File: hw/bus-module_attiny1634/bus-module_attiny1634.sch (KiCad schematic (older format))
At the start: 31 parts, among them J1 CONN_5X2, J2 CONN_5X2, J3 CONN-ISP-6, J4 CONN_1, J5 CONN_1, J6 CONN_1, J7 CONN_1, U1 7,3728MHz, U2 25LCXXX, U3 ATTINY1634-SOIC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

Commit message: R2, R3, R4 100 Ohms
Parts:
- C1, C2, C3, C4, C5, C7, R1, R2, R3, R4, R5, R6: footprint Resistor:SM0805 -> Resistor:R_0805
- F1: footprint (none) -> Resistor:R_1206
- U3: footprint SO20L -> Housings_SOIC:SO20L
- U5: footprint AM1S-XXXX_SIL4 -> DCDC_Converter:AM1S-XXXX_SIL4
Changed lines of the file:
@@
 F 0 "C7" H 7950 2250 50  0000 L CNN
 F 1 "100nF" H 7900 2075 50  0000 C CNN
-F 2 "Resistor:SM0805" H 7900 2200 60  0001 C CNN
+F 2 "Resistor:R_0805" H 7900 2200 60  0001 C CNN
 F 3 "" H 7900 2200 60  0000 C CNN
 	1    7900 2200
@@
 F 0 "C5" H 5650 2250 50  0000 L CNN
 F 1 "100nF" H 5600 2350 50  0000 C CNN
-F 2 "Resistor:SM0805" H 5600 2200 60  0001 C CNN
+F 2 "Resistor:R_0805" H 5600 2200 60  0001 C CNN
 F 3 "" H 5600 2200 60  0000 C CNN
 	1    5600 2200
@@
 F 0 "C3" H 5050 5200 50  0000 L CNN
 F 1 "18pF" H 5000 5025 50  0000 C CNN
-F 2 "Resistor:SM0805" H 5000 5150 60  0001 C CNN
+F 2 "Resistor:R_0805" H 5000 5150 60  0001 C CNN
 F 3 "" H 5000 5150 60  0000 C CNN
 	1    5000 5150
@@
 F 0 "C2" H 5050 4750 50  0000 L CNN
 F 1 "18pF" H 5000 4575 50  0000 C CNN
-F 2 "Resistor:SM0805" H 5000 4700 60  0001 C CNN
+F 2 "Resistor:R_0805" H 5000 4700 60  0001 C CNN
 F 3 "" H 5000 4700 60  0000 C CNN
 	1    5000 4700
@@
 F 0 "C4" H 5250 6350 50  0000 L CNN
 F 1 "100nF" H 5200 6175 50  0000 C CNN
-F 2 "Resistor:SM0805" H 5200 6300 60  0001 C CNN
+F 2 "Resistor:R_0805" H 5200 6300 60  0001 C CNN
 F 3 "" H 5200 6300 60  0000 C CNN
 	1    5200 6300
@@
 F 0 "R4" H 4100 5700 50  0000 C CNN
 F 1 "100" H 4800 5700 50  0000 C CNN
-F 2 "Resistor:SM0805" H 4800 5700 60  0001 C CNN
+F 2 "Resistor:R_0805" H 4800 5700 60  0001 C CNN
 F 3 "" H 4800 5700 60  0000 C CNN
 	1    4800 5700
@@
 F 0 "R3" H 4100 5600 50  0000 C CNN
 F 1 "100" H 4800 5600 50  0000 C CNN
-F 2 "Resistor:SM0805" H 4800 5600 60  0001 C CNN
+F 2 "Resistor:R_0805" H 4800 5600 60  0001 C CNN
 F 3 "" H 4800 5600 60  0000 C CNN
 	1    4800 5600
@@
 F 0 "R2" H 4100 5500 50  0000 C CNN
 F 1 "100" H 4800 5500 50  0000 C CNN
-F 2 "Resistor:SM0805" H 4800 5500 60  0001 C CNN
+F 2 "Resistor:R_0805" H 4800 5500 60  0001 C CNN
 F 3 "" H 4800 5500 60  0000 C CNN
 	1    4800 5500
@@
 F 0 "R1" H 4550 6250 50  0000 C CNN
 F 1 "10k" H 4550 6350 50  0000 C CNN
-F 2 "Resistor:SM0805" H 4550 6350 60  0001 C CNN
+F 2 "Resistor:R_0805" H 4550 6350 60  0001 C CNN
 F 3 "" H 4550 6350 60  0000 C CNN
 	1    4550 6350
@@
 F 0 "R6" H 5900 6250 50  0000 C CNN
 F 1 "10k" H 5900 6350 50  0000 C CNN
-F 2 "Resistor:SM0805" H 5900 6350 60  0001 C CNN
+F 2 "Resistor:R_0805" H 5900 6350 60  0001 C CNN
 F 3 "" H 5900 6350 60  0000 C CNN
 	1    5900 6350
@@
 F 0 "C1" H 4950 2250 50  0000 L CNN
 F 1 "4,7nF" H 5000 2350 50  0000 C CNN
-F 2 "Resistor:SM0805" H 4900 2200 60  0001 C CNN
+F 2 "Resistor:R_0805" H 4900 2200 60  0001 C CNN
 F 3 "" H 4900 2200 60  0000 C CNN
 	1    4900 2200
@@
 F 0 "R5" H 4900 1800 50  0000 C CNN
 F 1 "10k" H 4900 1700 50  0000 C CNN
-F 2 "Resistor:SM0805" H 4900 1700 60  0001 C CNN
+F 2 "Resistor:R_0805" H 4900 1700 60  0001 C CNN
 F 3 "" H 4900 1700 60  0000 C CNN
 	1    4900 1700
@@
 F 0 "U3" H 5350 3600 50  0000 C CNN
 F 1 "ATTINY1634-SOIC" H 5350 3000 50  0000 C CNN
-F 2 "SO20L" H 5350 3600 25  0001 C CNN
+F 2 "Housings_SOIC:SO20L" H 5350 3600 25  0001 C CNN
 F 3 "" H 5350 3600 25  0001 C CNN
 	1    5350 3600
@@
 F 0 "F1" H 9200 1300 50  0000 C CNN
 F 1 "FUSE" H 9200 1100 50  0000 C CNN
-F 2 "" H 9200 1200 60  0000 C CNN
+F 2 "Resistor:R_1206" H 9200 1200 60  0001 C CNN
 F 3 "" H 9200 1200 60  0000 C CNN
 	1    9200 1200
@@
 F 0 "U5" H 8050 1715 50  0000 C CNN
 F 1 "AM1S-2405" H 8050 1624 50  0000 C CNN
-F 2 "AM1S-XXXX_SIL4" H 8050 1500 25  0001 C CNN
+F 2 "DCDC_Converter:AM1S-XXXX_SIL4" H 8050 1500 25  0001 C CNN
 F 3 "" H 7300 1300 25  0001 C CNN
 	1    8050 1300

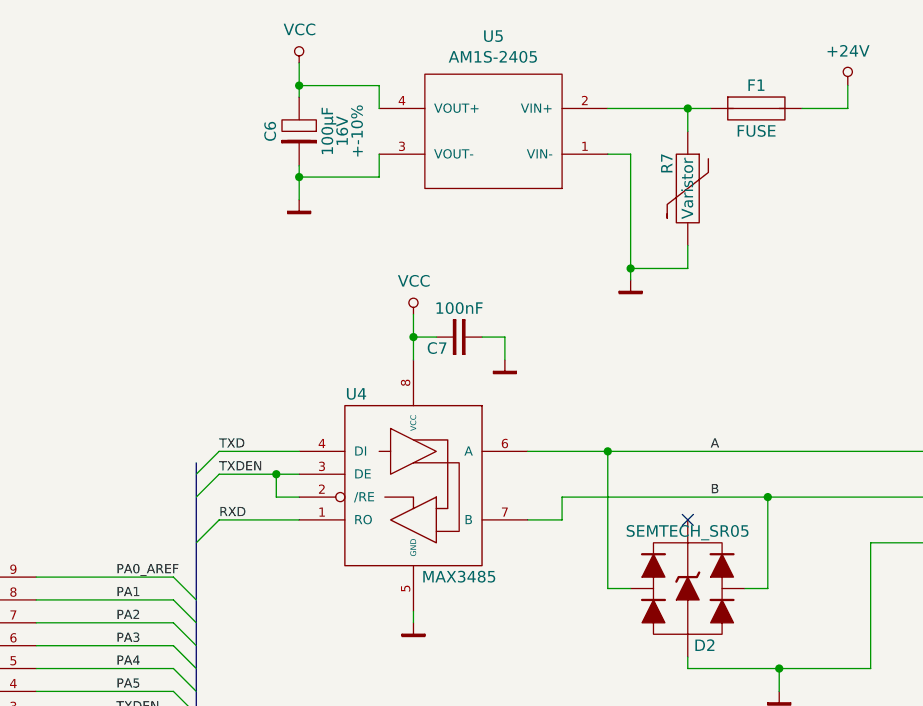
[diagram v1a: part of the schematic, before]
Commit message: Increase WAGO hole diameter, replace ELKO with keramic capacitor, Increase WAGO hole diameter, update footprints, update footprints, set Rev to C
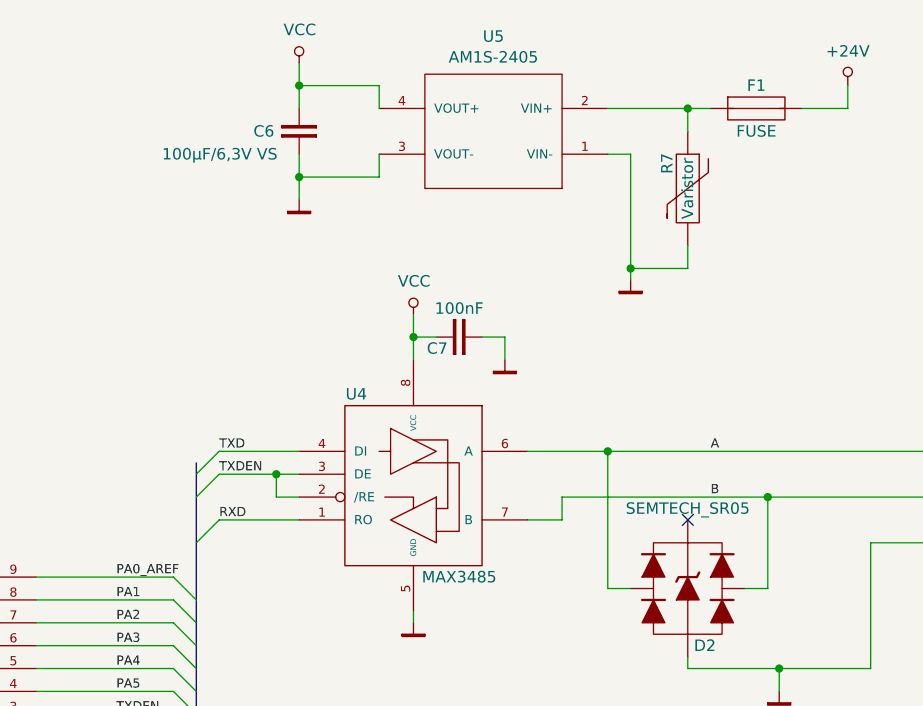
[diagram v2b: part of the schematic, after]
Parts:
- removed C6: 100µF, Capacitors:cp_smd_6.3, symbol standard:CP
- added C6: 100µF/6,3V VS, Capacitors_SMD:C_1206, symbol standard:C
- C1, C2, C3, C4, C5, C7: footprint Resistor:R_0805 -> Capacitors_SMD:C_0805
- D1: footprint Diode:SOD323 -> Diode_SMD:D_SOD323
- D2: footprint Diode_SMD:SOT143 -> Diode_SMD:D_SOT143
- J4, J5, J6, J7: footprint Connector_Miscelleaneus:WAGO243 -> Connector_WAGO:WAGO243
- U1: footprint Crystal:HC49-SMD -> Crystal:CRY_HC49_SMD
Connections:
- net GND: now also C6.2
- net VCC: now also C6.1
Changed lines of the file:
@@
 Sheet 1 1
 Title "bus-module_attiny1634"
-Date "2018-09-24"
-Rev "B"
+Date "2019-03-06"
+Rev "C"
 Comp "KoeWiBa"
 Comment1 ""
@@
 F 0 "J4" H 10400 2575 50  0000 C CNN
 F 1 "CONN_1" H 10400 2425 25  0000 C CNN
-F 2 "Connector_Miscelleaneus:WAGO243" H 10400 2500 60  0001 C CNN
+F 2 "Connector_WAGO:WAGO243" H 10400 2500 60  0001 C CNN
 F 3 "" H 10400 2500 60  0000 C CNN
 	1    10400 2500
@@
 F 0 "J5" H 10400 2775 50  0000 C CNN
 F 1 "CONN_1" H 10400 2625 25  0000 C CNN
-F 2 "Connector_Miscelleaneus:WAGO243" H 10400 2700 60  0001 C CNN
+F 2 "Connector_WAGO:WAGO243" H 10400 2700 60  0001 C CNN
 F 3 "" H 10400 2700 60  0000 C CNN
 	1    10400 2700
@@
 F 0 "J6" H 10400 2975 50  0000 C CNN
 F 1 "CONN_1" H 10400 2825 25  0000 C CNN
-F 2 "Connector_Miscelleaneus:WAGO243" H 10400 2900 60  0001 C CNN
+F 2 "Connector_WAGO:WAGO243" H 10400 2900 60  0001 C CNN
 F 3 "" H 10400 2900 60  0000 C CNN
 	1    10400 2900
@@
 F 0 "J7" H 10400 3175 50  0000 C CNN
 F 1 "CONN_1" H 10400 3025 25  0000 C CNN
-F 2 "Connector_Miscelleaneus:WAGO243" H 10400 3100 60  0001 C CNN
+F 2 "Connector_WAGO:WAGO243" H 10400 3100 60  0001 C CNN
 F 3 "" H 10400 3100 60  0000 C CNN
 	1    10400 3100
 	1    0    0    -1
-$EndComp
-$Comp
-L standard:CP C6
-U 1 1 559D5D78
-P 7200 1300
-F 0 "C6" H 7200 1175 50  0000 C CNN
-F 1 "100µF" H 7200 1425 50  0000 C CNN
-F 2 "Capacitors:cp_smd_6.3" H 7200 1300 60  0001 C CNN
-F 3 "" H 7200 1300 60  0000 C CNN
-F 4 "16V" H 7200 1490 50  0000 C CNN "Voltage"
-F 5 "+-10%" H 7200 1555 50  0000 C CNN "Tolrance"
-	1    7200 1300
-	0    1    1    0
 $EndComp
 $Comp
@@
 F 0 "C7" H 7950 2250 50  0000 L CNN
 F 1 "100nF" H 7900 2075 50  0000 C CNN
-F 2 "Resistor:R_0805" H 7900 2200 60  0001 C CNN
+F 2 "Capacitors_SMD:C_0805" H 7900 2200 60  0001 C CNN
 F 3 "" H 7900 2200 60  0000 C CNN
 	1    7900 2200
@@
 F 0 "C5" H 5650 2250 50  0000 L CNN
 F 1 "100nF" H 5600 2350 50  0000 C CNN
-F 2 "Resistor:R_0805" H 5600 2200 60  0001 C CNN
+F 2 "Capacitors_SMD:C_0805" H 5600 2200 60  0001 C CNN
 F 3 "" H 5600 2200 60  0000 C CNN
 	1    5600 2200
@@
 F 0 "C3" H 5050 5200 50  0000 L CNN
 F 1 "18pF" H 5000 5025 50  0000 C CNN
-F 2 "Resistor:R_0805" H 5000 5150 60  0001 C CNN
+F 2 "Capacitors_SMD:C_0805" H 5000 5150 60  0001 C CNN
 F 3 "" H 5000 5150 60  0000 C CNN
 	1    5000 5150
@@
 F 0 "C2" H 5050 4750 50  0000 L CNN
 F 1 "18pF" H 5000 4575 50  0000 C CNN
-F 2 "Resistor:R_0805" H 5000 4700 60  0001 C CNN
+F 2 "Capacitors_SMD:C_0805" H 5000 4700 60  0001 C CNN
 F 3 "" H 5000 4700 60  0000 C CNN
 	1    5000 4700
@@
 F 0 "C4" H 5250 6350 50  0000 L CNN
 F 1 "100nF" H 5200 6175 50  0000 C CNN
-F 2 "Resistor:R_0805" H 5200 6300 60  0001 C CNN
+F 2 "Capacitors_SMD:C_0805" H 5200 6300 60  0001 C CNN
 F 3 "" H 5200 6300 60  0000 C CNN
 	1    5200 6300
@@
 F 0 "U1" H 4925 4850 50  0000 C CNN
 F 1 "7,3728MHz" H 4925 4650 50  0000 C CNN
-F 2 "Crystal:HC49-SMD" H 4750 4750 60  0001 C CNN
+F 2 "Crystal:CRY_HC49_SMD" H 4750 4750 60  0001 C CNN
 F 3 "" H 4750 4750 60  0000 C CNN
 	1    4750 4750
@@
 F 0 "C1" H 4950 2250 50  0000 L CNN
 F 1 "4,7nF" H 5000 2350 50  0000 C CNN
-F 2 "Resistor:R_0805" H 4900 2200 60  0001 C CNN
+F 2 "Capacitors_SMD:C_0805" H 4900 2200 60  0001 C CNN
 F 3 "" H 4900 2200 60  0000 C CNN
 	1    4900 2200
@@
 F 0 "D1" H 4660 1780 50  0000 C CNN
 F 1 "1N4148WS (SOD323)" H 4950 1600 50  0000 C CNN
-F 2 "Diode:SOD323" H 4650 1700 60  0001 C CNN
+F 2 "Diode_SMD:D_SOD323" H 4650 1700 60  0001 C CNN
 F 3 "" H 4650 1700 60  0000 C CNN
 	1    4650 1700
@@
 	7550 1500 7200 1500
 Wire Wire Line
-	7200 1450 7200 1500
-Wire Wire Line
 	10300 3100 9700 3100
 Wire Wire Line
@@
 Wire Wire Line
 	8650 1400 8650 1900
-Connection ~ 7200 1500
-Connection ~ 7200 1100
 Wire Wire Line
 	6050 3250 6650 3250
@@
 P 8900 3300
 F 0 "D2" H 8975 3050 50  0000 C CNN
-F 1 "SEMTECH_SR05" H 8900 3550 50  0000 C CNN
-F 2 "Diode_SMD:SOT143" H 8900 3300 60  0001 C CNN
+F 1 "SEMTECH_SR05" H 8900 3650 50  0000 C CNN
+F 2 "Diode_SMD:D_SOT143" H 8900 3300 60  0001 C CNN
 F 3 "" H 8900 3300 60  0000 C CNN
 	1    8900 3300
@@
 	7200 1500 7200 1600
 Wire Wire Line
-	7200 1100 7200 1150
-Wire Wire Line
 	8550 2700 10300 2700
 Wire Wire Line
@@
 	-1   0    0    -1
 $EndComp
+$Comp
+L standard:C C6
+U 1 1 5C8087D1
+P 7200 1300
+F 0 "C6" V 7200 1100 50  0000 L CNN
+F 1 "100µF/6,3V VS" V 7300 700 50  0000 L CNN
+F 2 "Capacitors_SMD:C_1206" H 7200 1300 60  0001 C CNN
+F 3 "" H 7200 1300 60  0000 C CNN
+	1    7200 1300
+	0    1    1    0
+$EndComp
+Wire Wire Line
+	7200 1200 7200 1100
+Connection ~ 7200 1100
+Wire Wire Line
+	7200 1400 7200 1500
+Connection ~ 7200 1500
 Wire Bus Line
 	5300 5600 5300 5800
